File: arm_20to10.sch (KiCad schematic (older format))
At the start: 10 parts, among them J1 ARM_20PIN, J2 ARM_10PIN, P1 +5V, P2 VCC, P3 GND, P4 GND, SW1 DUAL_SWITCH_INV, U1 AAT3221 or LP5907

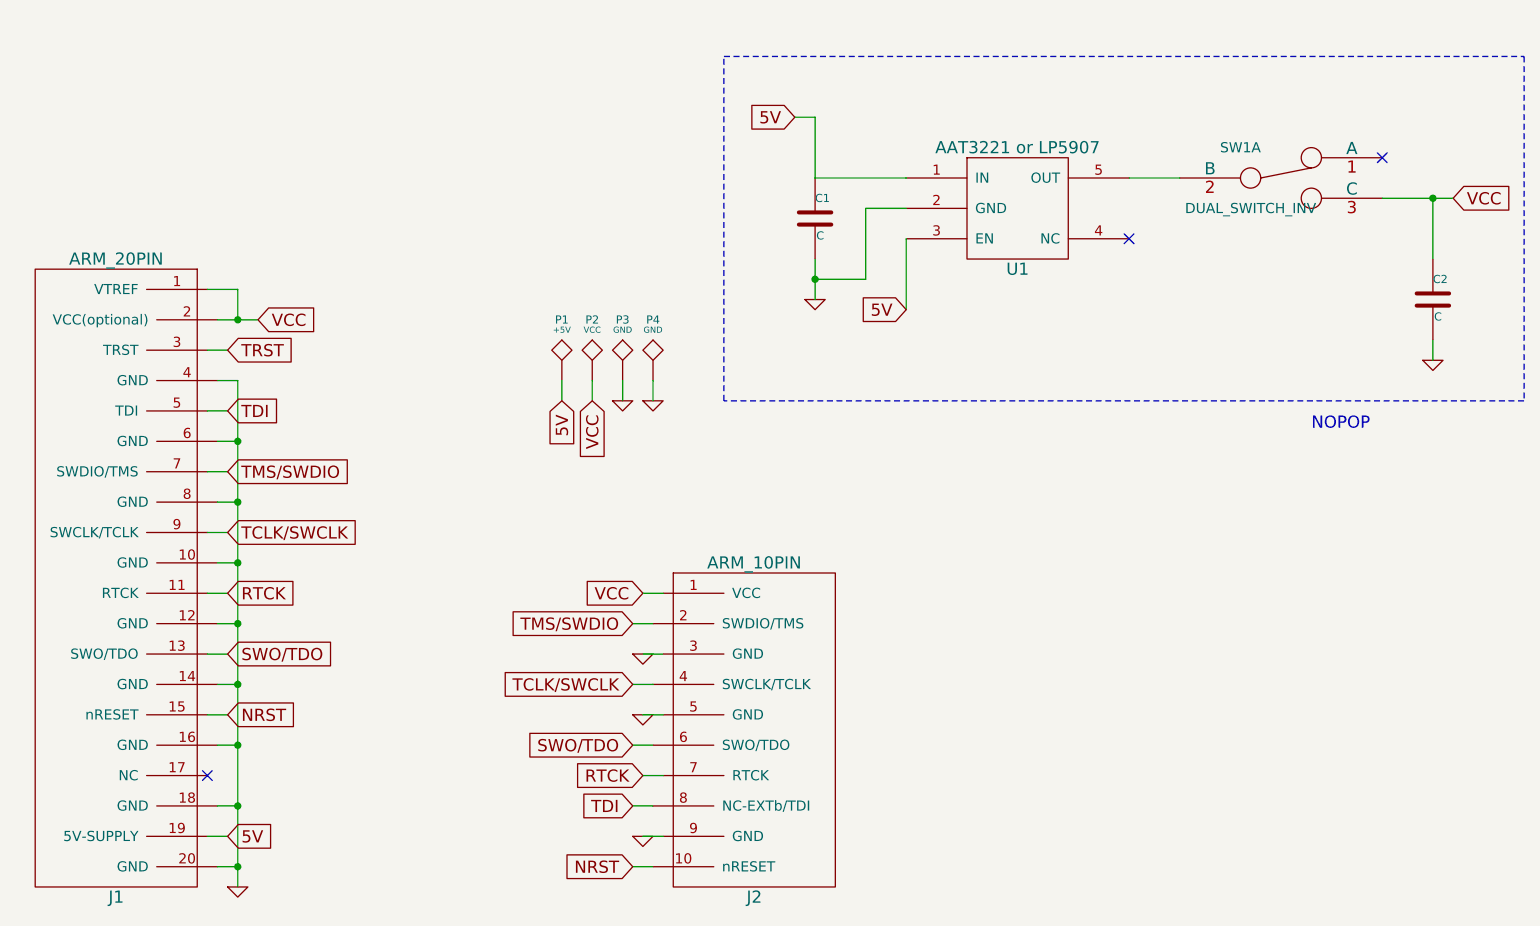
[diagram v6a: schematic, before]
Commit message: - new layout w/ ldo + switch
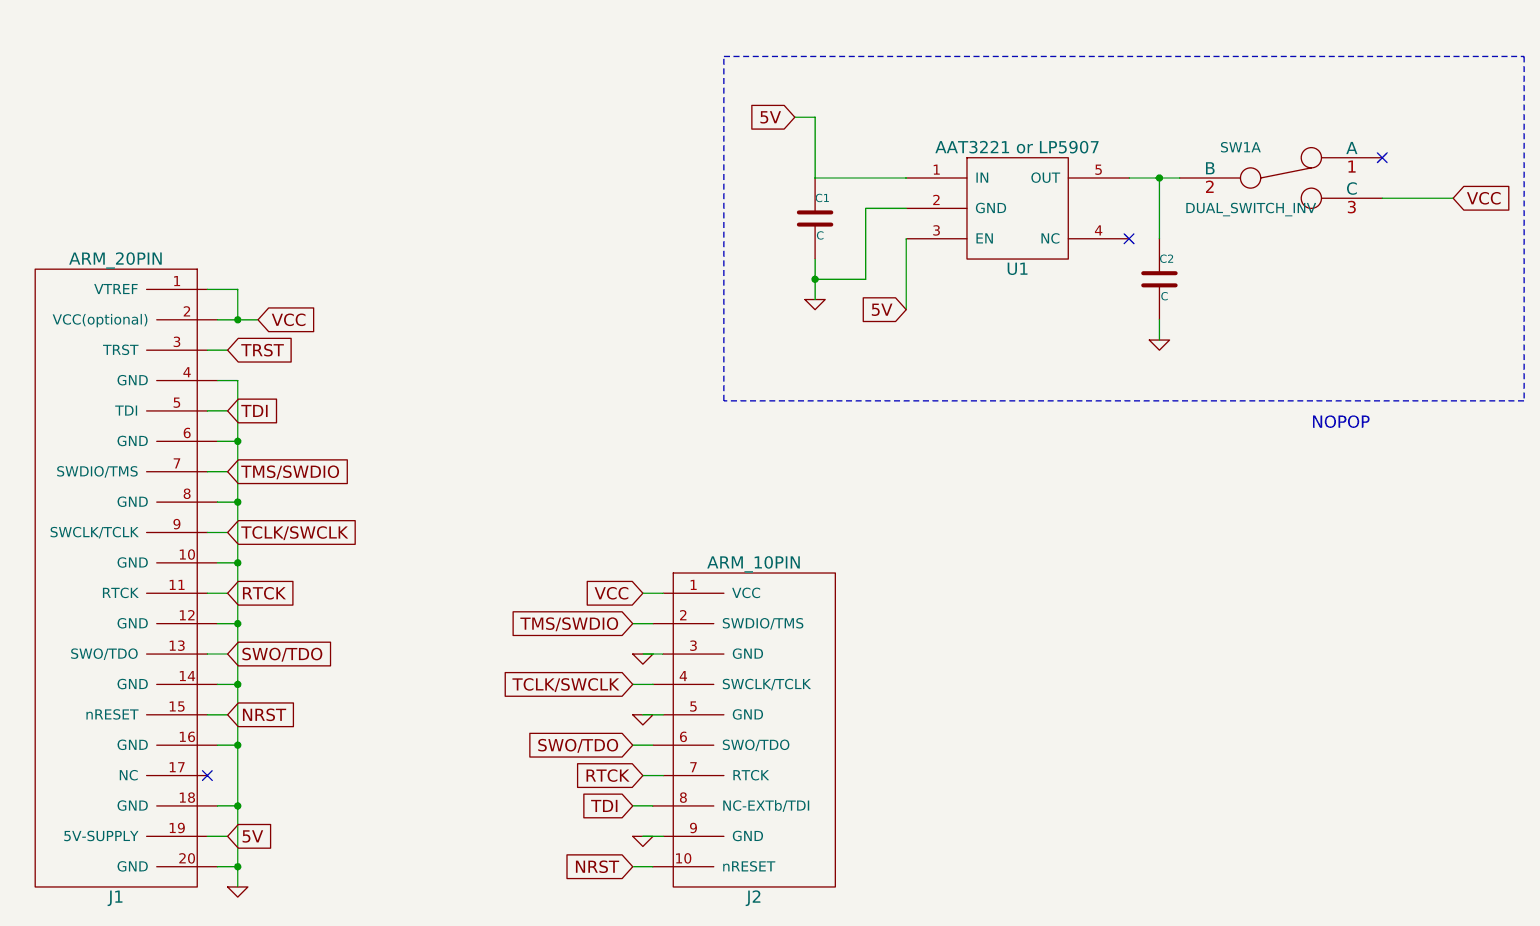
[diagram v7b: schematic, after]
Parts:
- removed P1: +5V, ~, symbol TST
- removed P2: VCC, ~, symbol TST
- removed P3, P4: GND, ~, symbol TST
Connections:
- net VCC: no longer C2.1
- net at SW1.2 (B), U1.5 (OUT): now also C2.1
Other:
- moved on the sheet: C2
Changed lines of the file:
@@
 Wire Wire Line
 	5950 4800 6050 4800
-$Comp
-L TST P1
-U 1 1 52E9A2C6
-P 5600 2700
-F 0 "P1" H 5600 3000 40  0000 C CNN
-F 1 "+5V" H 5600 2950 30  0000 C CNN
-F 2 "~" H 5600 2700 60  0000 C CNN
-F 3 "~" H 5600 2700 60  0000 C CNN
-	1    5600 2700
-	1    0    0    -1
-$EndComp
 Text GLabel 3950 4950 2    60   Input ~ 0
 5V
@@
 Connection ~ 4000 2400
 NoConn ~ 3850 4650
-Text GLabel 5750 2800 3    60   Input ~ 0
-VCC
-$Comp
-L TST P2
-U 1 1 52E9A439
-P 5750 2700
-F 0 "P2" H 5750 3000 40  0000 C CNN
-F 1 "VCC" H 5750 2950 30  0000 C CNN
-F 2 "~" H 5750 2700 60  0000 C CNN
-F 3 "~" H 5750 2700 60  0000 C CNN
-	1    5750 2700
-	1    0    0    -1
-$EndComp
-Text GLabel 5600 2800 3    60   Input ~ 0
-5V
-Wire Wire Line
-	5600 2800 5600 2700
-Wire Wire Line
-	5750 2700 5750 2800
-$Comp
-L GND #PWR03
-U 1 1 52E9A4EA
-P 5900 2800
-F 0 "#PWR03" H 5900 2800 30  0001 C CNN
-F 1 "GND" H 5900 2730 30  0001 C CNN
-F 2 "" H 5900 2800 60  0000 C CNN
-F 3 "" H 5900 2800 60  0000 C CNN
-	1    5900 2800
-	1    0    0    -1
-$EndComp
-$Comp
-L TST P3
-U 1 1 52E9A4F0
-P 5900 2700
-F 0 "P3" H 5900 3000 40  0000 C CNN
-F 1 "GND" H 5900 2950 30  0000 C CNN
-F 2 "~" H 5900 2700 60  0000 C CNN
-F 3 "~" H 5900 2700 60  0000 C CNN
-	1    5900 2700
-	1    0    0    -1
-$EndComp
-Wire Wire Line
-	5900 2700 5900 2800
 Text GLabel 3950 3750 2    60   Input ~ 0
 RTCK
@@
 RTCK
 $Comp
-L GND #PWR04
+L GND #PWR03
 U 1 1 52E9A6FB
 P 6000 4350
-F 0 "#PWR04" H 6000 4350 30  0001 C CNN
+F 0 "#PWR03" H 6000 4350 30  0001 C CNN
 F 1 "GND" H 6000 4280 30  0001 C CNN
 F 2 "" H 6000 4350 60  0000 C CNN
@@
 TCLK/SWCLK
 $Comp
-L GND #PWR05
+L GND #PWR04
 U 1 1 52E9A838
 P 6000 4050
-F 0 "#PWR05" H 6000 4050 30  0001 C CNN
+F 0 "#PWR04" H 6000 4050 30  0001 C CNN
 F 1 "GND" H 6000 3980 30  0001 C CNN
 F 2 "" H 6000 4050 60  0000 C CNN
@@
 	1    0    0    -1
 $EndComp
-$Comp
-L GND #PWR06
-U 1 1 52EBCB6E
-P 6050 2800
-F 0 "#PWR06" H 6050 2800 30  0001 C CNN
-F 1 "GND" H 6050 2730 30  0001 C CNN
-F 2 "" H 6050 2800 60  0000 C CNN
-F 3 "" H 6050 2800 60  0000 C CNN
-	1    6050 2800
-	1    0    0    -1
-$EndComp
-$Comp
-L TST P4
-U 1 1 52EBCB74
-P 6050 2700
-F 0 "P4" H 6050 3000 40  0000 C CNN
-F 1 "GND" H 6050 2950 30  0000 C CNN
-F 2 "~" H 6050 2700 60  0000 C CNN
-F 3 "~" H 6050 2700 60  0000 C CNN
-	1    6050 2700
-	1    0    0    -1
-$EndComp
-Wire Wire Line
-	6050 2700 6050 2800
 $Comp
 L AAT3221 U1
@@
 L C C2
 U 1 1 52FC3072
-P 9900 2300
-F 0 "C2" H 9900 2400 40  0000 L CNN
-F 1 "C" H 9906 2215 40  0000 L CNN
-F 2 "~" H 9938 2150 30  0000 C CNN
-F 3 "~" H 9900 2300 60  0000 C CNN
-	1    9900 2300
+P 8550 2200
+F 0 "C2" H 8550 2300 40  0000 L CNN
+F 1 "C" H 8556 2115 40  0000 L CNN
+F 2 "~" H 8588 2050 30  0000 C CNN
+F 3 "~" H 8550 2200 60  0000 C CNN
+	1    8550 2200
 	1    0    0    -1
 $EndComp
@@
 	6850 1700 7300 1700
 $Comp
-L GND #PWR07
+L GND #PWR05
 U 1 1 52FC3225
 P 6850 2300
-F 0 "#PWR07" H 6850 2300 30  0001 C CNN
+F 0 "#PWR05" H 6850 2300 30  0001 C CNN
 F 1 "GND" H 6850 2230 30  0001 C CNN
 F 2 "" H 6850 2300 60  0000 C CNN
@@
 	7300 2000 7300 2350
 $Comp
-L GND #PWR08
+L GND #PWR06
 U 1 1 52FC3410
-P 9900 2600
-F 0 "#PWR08" H 9900 2600 30  0001 C CNN
-F 1 "GND" H 9900 2530 30  0001 C CNN
-F 2 "" H 9900 2600 60  0000 C CNN
-F 3 "" H 9900 2600 60  0000 C CNN
-	1    9900 2600
+P 8550 2500
+F 0 "#PWR06" H 8550 2500 30  0001 C CNN
+F 1 "GND" H 8550 2430 30  0001 C CNN
+F 2 "" H 8550 2500 60  0000 C CNN
+F 3 "" H 8550 2500 60  0000 C CNN
+	1    8550 2500
 	1    0    0    -1
 $EndComp
 Wire Wire Line
-	9900 2600 9900 2500
+	8550 2500 8550 2400
 Text GLabel 10000 1800 2    60   Input ~ 0
 VCC
-Wire Wire Line
-	9650 1800 10000 1800
-Wire Wire Line
-	9900 1800 9900 2100
 $Comp
 L DUAL_SWITCH_INV SW1
@@
 Wire Wire Line
 	8650 1700 8400 1700
-Connection ~ 9900 1800
 Wire Notes Line
 	6400 1100 10350 1100
@@
 Text Notes 9300 2950 0    60   ~ 0
 NOPOP
+Wire Wire Line
+	10000 1800 9650 1800
+Wire Wire Line
+	8550 2000 8550 1700
+Connection ~ 8550 1700
 $EndSCHEMATC

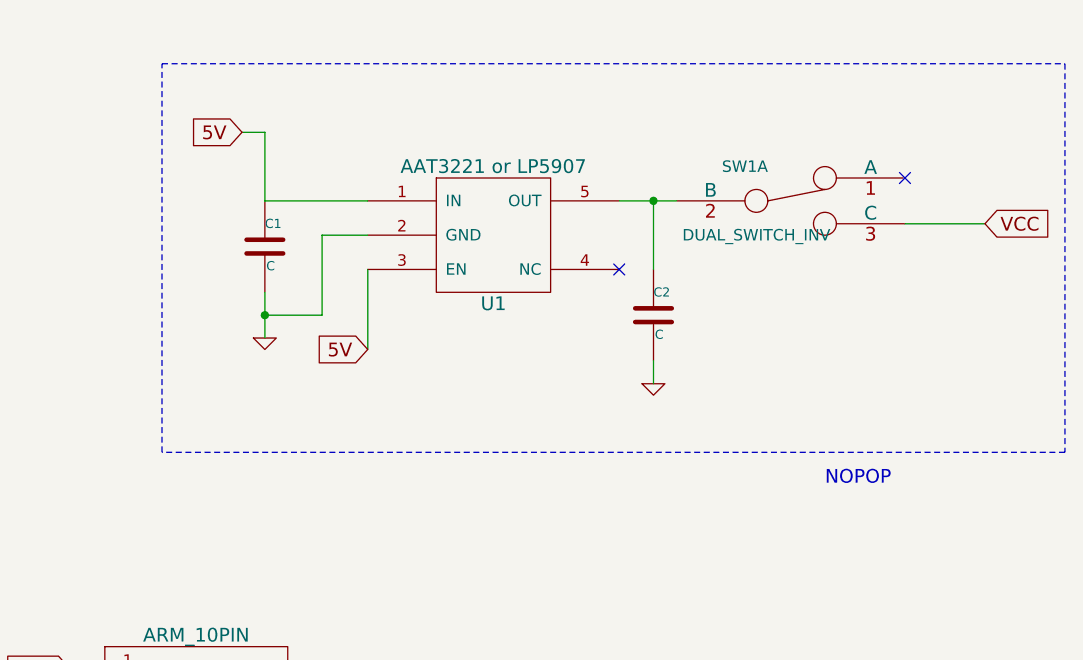
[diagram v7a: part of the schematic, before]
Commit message: - add power indicator leds
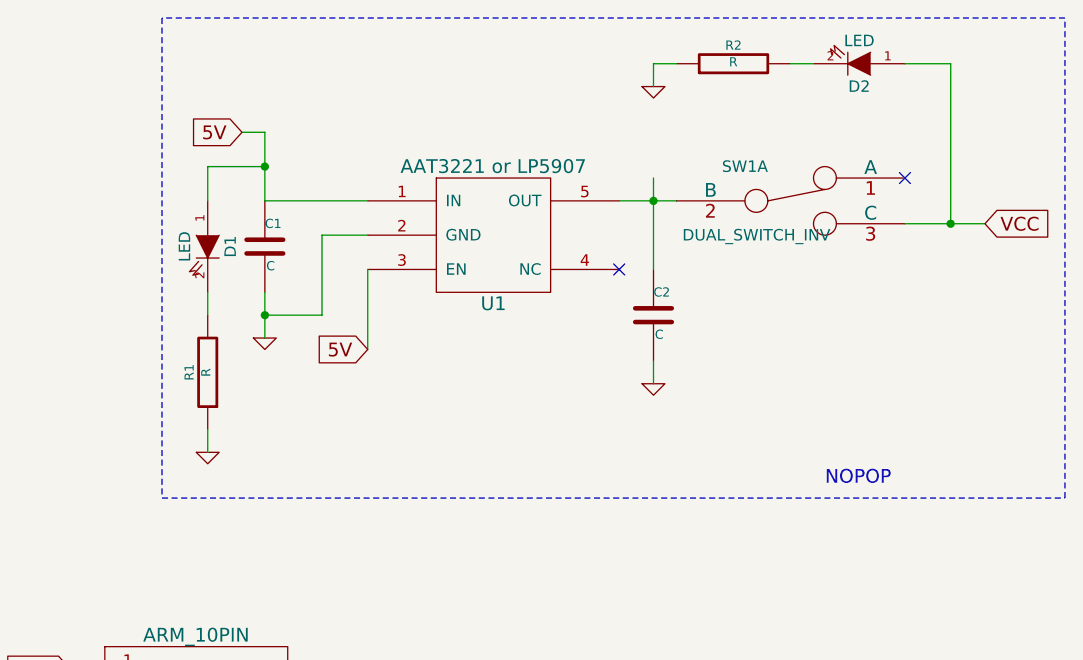
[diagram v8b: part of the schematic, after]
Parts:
- added D1, D2: LED, ~, symbol LED
- added R1, R2: R, ~, symbol R
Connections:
- net 5V: now also D1.1 (A)
- net GND: now also R1.1, R2.1
- net VCC: now also D2.1 (A)
- new net: D2.2 (K), R2.2
- new net: D1.2 (K), R1.2
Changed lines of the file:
@@
 Sheet 1 1
 Title ""
-Date "20 feb 2014"
+Date "8 mar 2014"
 Rev ""
 Comp ""
@@
 Wire Wire Line
 	8650 1700 8400 1700
-Wire Notes Line
-	6400 1100 10350 1100
-Wire Notes Line
-	10350 1100 10350 2800
-Wire Notes Line
-	10350 2800 6400 2800
-Wire Notes Line
-	6400 2800 6400 1100
 Text Notes 9300 2950 0    60   ~ 0
 NOPOP
@@
 	10000 1800 9650 1800
 Wire Wire Line
-	8550 2000 8550 1700
+	8550 1600 8550 2000
 Connection ~ 8550 1700
+$Comp
+L LED D2
+U 1 1 531B4083
+P 9450 1100
+F 0 "D2" H 9450 1200 50  0000 C CNN
+F 1 "LED" H 9450 1000 50  0000 C CNN
+F 2 "~" H 9450 1100 60  0000 C CNN
+F 3 "~" H 9450 1100 60  0000 C CNN
+	1    9450 1100
+	-1   0    0    1
+$EndComp
+$Comp
+L R R2
+U 1 1 531B40CC
+P 8900 1100
+F 0 "R2" V 8980 1100 40  0000 C CNN
+F 1 "R" V 8907 1101 40  0000 C CNN
+F 2 "~" V 8830 1100 30  0000 C CNN
+F 3 "~" H 8900 1100 30  0000 C CNN
+	1    8900 1100
+	0    -1   -1   0
+$EndComp
+Wire Wire Line
+	8650 1100 8550 1100
+Wire Wire Line
+	8550 1100 8550 1200
+$Comp
+L GND #PWR07
+U 1 1 531B4113
+P 8550 1200
+F 0 "#PWR07" H 8550 1200 30  0001 C CNN
+F 1 "GND" H 8550 1130 30  0001 C CNN
+F 2 "" H 8550 1200 60  0000 C CNN
+F 3 "" H 8550 1200 60  0000 C CNN
+	1    8550 1200
+	1    0    0    -1
+$EndComp
+Wire Wire Line
+	9250 1100 9150 1100
+Wire Notes Line
+	10350 900  6400 900
+$Comp
+L LED D1
+U 1 1 531B42E2
+P 6600 1900
+F 0 "D1" H 6600 2000 50  0000 C CNN
+F 1 "LED" H 6600 1800 50  0000 C CNN
+F 2 "~" H 6600 1900 60  0000 C CNN
+F 3 "~" H 6600 1900 60  0000 C CNN
+	1    6600 1900
+	0    1    1    0
+$EndComp
+$Comp
+L R R1
+U 1 1 531B42E8
+P 6600 2450
+F 0 "R1" V 6680 2450 40  0000 C CNN
+F 1 "R" V 6607 2451 40  0000 C CNN
+F 2 "~" V 6530 2450 30  0000 C CNN
+F 3 "~" H 6600 2450 30  0000 C CNN
+	1    6600 2450
+	-1   0    0    1
+$EndComp
+$Comp
+L GND #PWR08
+U 1 1 531B42EE
+P 6600 2800
+F 0 "#PWR08" H 6600 2800 30  0001 C CNN
+F 1 "GND" H 6600 2730 30  0001 C CNN
+F 2 "" H 6600 2800 60  0000 C CNN
+F 3 "" H 6600 2800 60  0000 C CNN
+	1    6600 2800
+	1    0    0    -1
+$EndComp
+Wire Notes Line
+	6400 3000 10350 3000
+Wire Notes Line
+	10350 3000 10350 900
+Wire Notes Line
+	6400 900  6400 3000
+Wire Wire Line
+	6600 2700 6600 2800
+Wire Wire Line
+	6600 2100 6600 2200
+Wire Wire Line
+	6600 1700 6600 1550
+Wire Wire Line
+	6600 1550 6850 1550
+Connection ~ 6850 1550
+Wire Wire Line
+	9650 1100 9850 1100
+Wire Wire Line
+	9850 1100 9850 1800
+Connection ~ 9850 1800
 $EndSCHEMATC
